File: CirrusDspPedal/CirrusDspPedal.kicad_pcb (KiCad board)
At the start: 2 copper layers, 112.5 x 86.4 mm, 89 parts, among them J1 MonoJack2Switch, J2 MonoJack2Switch, J3 Conn_02x05_Odd_Even, J4 Barrel_Jack_Switch, J5 MonoJack2Switch, J6 Micro_SD_Card_Det, J7 Conn_01x01, K1 HFD4/5-S, SW1 P26L-1D-RND MTL, SW2 P26L-1D-RND MTL, SW3 SW_SPST, SW4 SW_SPST, U1 CS5343, U2 74AHC1G126, U3 CS4344, U5 MCP1703T-3302E/CB, U6 MCP601-xOT, U7 STM32F405RGTx

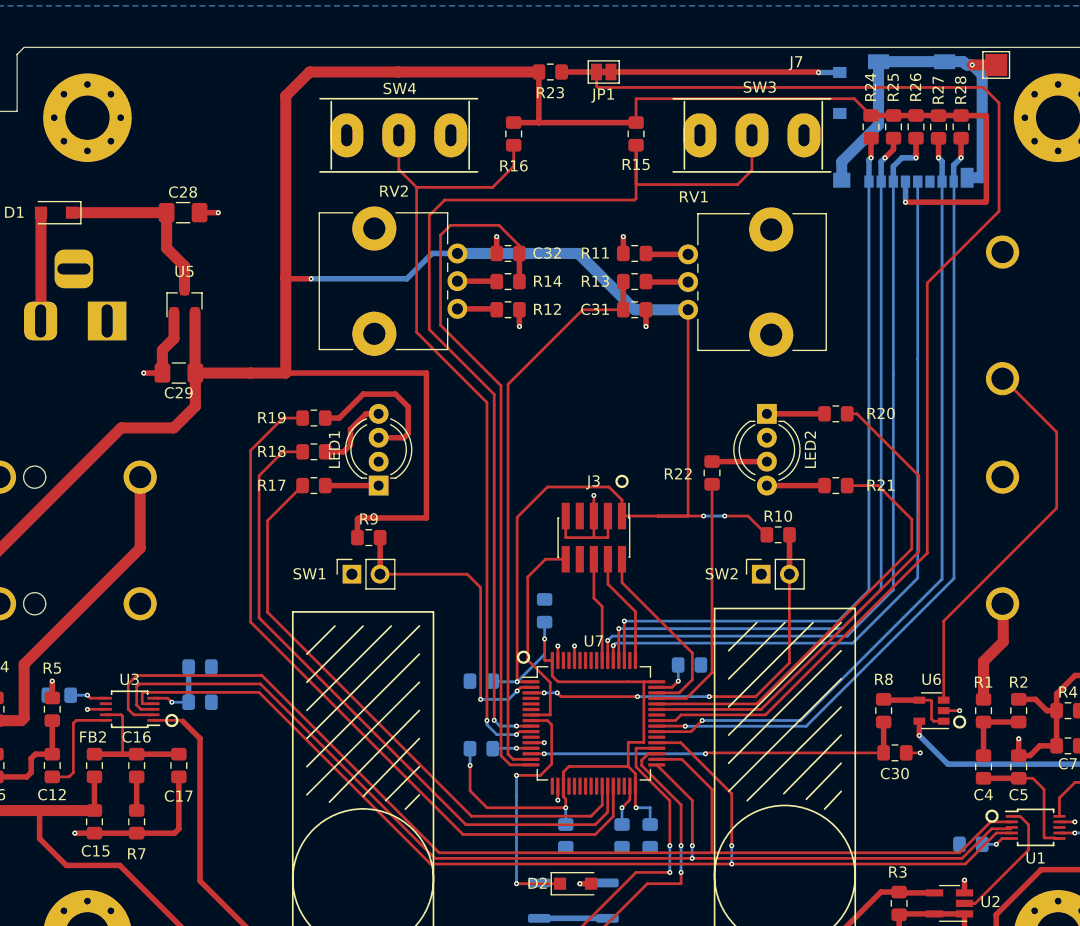
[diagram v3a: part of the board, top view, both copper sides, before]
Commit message: updated design and layout
- Changed LDO package from SOT23 to SOT223
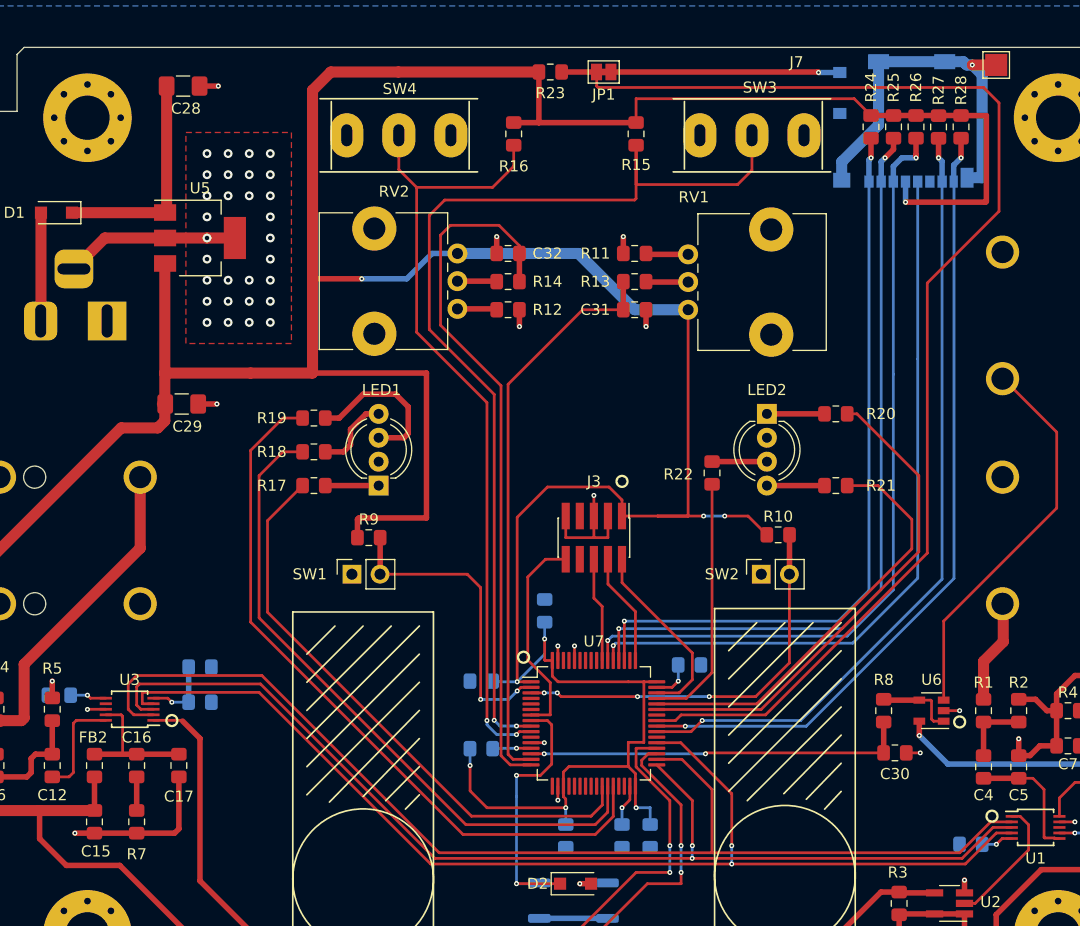
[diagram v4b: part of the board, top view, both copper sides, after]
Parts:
- U5: value MCP1703T-3302E/CB -> MCP1703A-1202_SOT223; footprint Package_TO_SOT_SMD:SOT-23 -> Package_TO_SOT_SMD:SOT-223-3_TabPin2
- moved C28 11.4 mm to (113.4, 58.0)
- moved U5 5.88 mm to (114.9, 71.8), turned to 0 degrees
- moved C29 2.81 mm to (113.3, 86.7), turned to 0 degrees
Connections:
- U5 pad 1: GND -> Net-(C28-Pad1)
- U5 pad 2: +3V3 -> GND
- U5 pad 3: Net-(C28-Pad1) -> +3V3
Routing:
- net GND: track 77.6 -> 87.4 mm, vias 22 -> 52
- net Net-(C28-Pad1): track 16.2 -> 19.9 mm
- net +3V3: track 562.4 -> 565.7 mm
- added copper zone on F.Cu, net GND

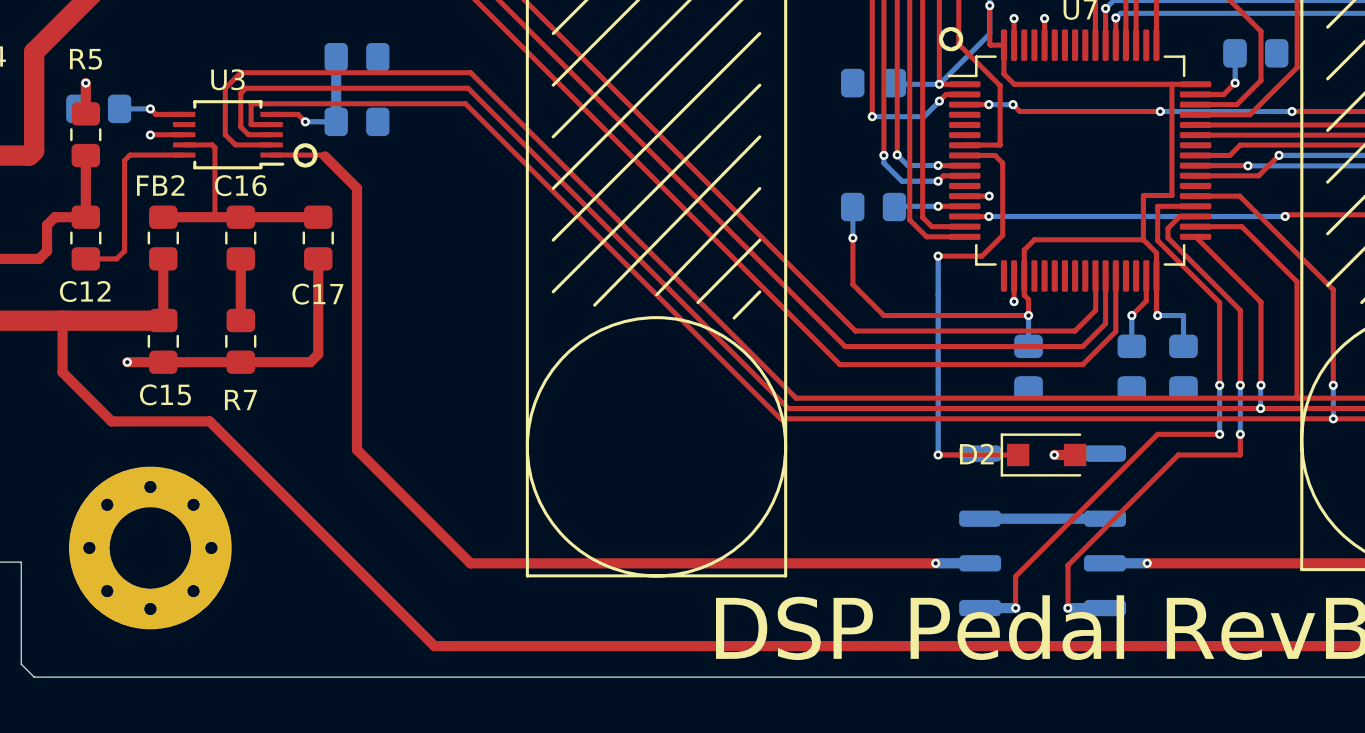
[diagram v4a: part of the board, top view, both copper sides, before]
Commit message: Updated design
- Corrected trace going to wrong CS4344 channel output
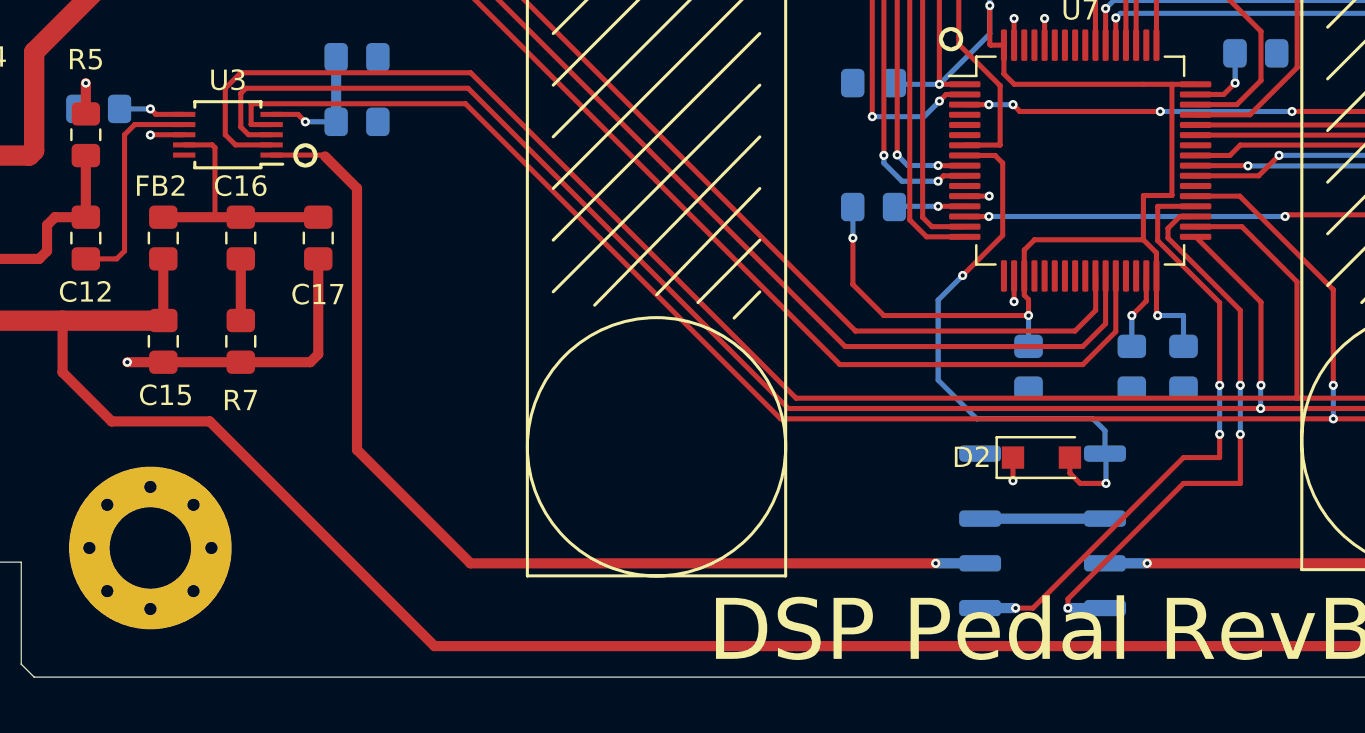
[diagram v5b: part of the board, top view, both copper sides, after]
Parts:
- moved D2 0.28 mm to (148.6, 130.2)
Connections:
- D2 pad 1: /SignalProcessing/RelayCoil_OUT -> GND
- D2 pad 2: GND -> /SignalProcessing/RelayCoil_OUT
- K1 pad 1: GND -> /SignalProcessing/RelayCoil_OUT
- K1 pad 8: /SignalProcessing/RelayCoil_OUT -> GND
- U3 pad 10: Net-(C12-Pad2) -> Net-(U3-Pad10)
- U3 pad 7: Net-(U3-Pad7) -> Net-(C12-Pad2)
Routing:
- net /SignalProcessing/RelayCoil_OUT: track 25.3 -> 28.9 mm
- net Net-(C12-Pad2): track 9.55 -> 10.9 mm

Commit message: finished revb layout
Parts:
- added C23: 1uF, Capacitor_SMD:C_1206_3216Metric_Pad1.42x1.75mm_HandSolder, F.Cu at (95.2, 87.6)
- added C24: 1uF, Capacitor_SMD:C_1206_3216Metric_Pad1.42x1.75mm_HandSolder, F.Cu at (104.1, 87.6)
- added U4: SE8250X2_SOT23, Package_TO_SOT_SMD:SOT-23, F.Cu at (99.7, 87.6)
- C18, C19, C21, C22, C33: moved to F.Cu
- K1: value HFD4/5-S -> HFD4/3_S
- moved C6 21.1 mm to (199.8, 124.1), turned to 270 degrees
- moved R3 17.7 mm to (195.3, 128.1), turned to 0 degrees
- moved U2 14.8 mm to (195.3, 124.4), turned to 270 degrees
- moved C30 14.3 mm to (180.8, 104.3), turned to 270 degrees
- moved C18 8.63 mm to (146.2, 105.4), turned to 90 degrees
- moved R8 7.40 mm to (180.8, 108.3), turned to 270 degrees
- moved C1 6.35 mm to (190.1, 123.1)
- moved C2 6.35 mm to (190.1, 125.5)
- moved C3 6.35 mm to (178.2, 126.5)
- moved U1 6.35 mm to (184.0, 125.0)
- moved C33 3.82 mm to (156.3, 107.7), turned to 270 degrees
- moved C21 2.67 mm to (148.7, 105.4)
- moved C12 2.54 mm to (104.1, 119.4)
- moved C13 2.54 mm to (104.8, 113.0)
- moved C14 2.54 mm to (99.1, 114.3)
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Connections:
- C15 pad 1: +3V3 -> +5V
- C6 pad 1: +3V3 -> +5V
- C7 pad 1: +3V3 -> +5V
- FB1 pad 2: +3V3 -> +5V
- FB2 pad 2: +3V3 -> +5V
- R3 pad 2: +3V3 -> +5V
- U2 pad 1: +3V3 -> +5V
- U2 pad 5: +3V3 -> +5V
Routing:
- net +5V: track 0.00 -> 183.5 mm, vias 0 -> 2
- net +3V3: track 565.7 -> 393.7 mm, vias 12 -> 13
- net Net-(C23-Pad1): track 19.9 -> 53.7 mm
- net /InputSignal/ADIN_LRCK: track 99.9 -> 131.7 mm
- net /InputSignal/ADIN_SCLK: track 104.5 -> 135.7 mm
- net /InputSignal/ADIN_MCLK: track 103.1 -> 132.8 mm, vias 2 -> 5
- net /ExtInput/FootExp_IN: track 34.9 -> 61.2 mm
- net GND: track 87.5 -> 113.1 mm, vias 52 -> 56
- net /InputSignal/ADIN_SDOUT: track 31.5 -> 52.9 mm
- net /InputSignal/SDOUT: track 11.9 -> 22.3 mm
- net /MicroSD/uSD_CMD: track 71.8 -> 62.3 mm
- net /MicroSD/uSD_D3: track 69.2 -> 60.6 mm
- net /MicroSD/uSD_CLK: track 67.1 -> 58.6 mm
- net /SignalProcessing/LEDA_R: track 52.7 -> 61.3 mm
- net /MicroSD/uSD_D2: track 67.9 -> 59.8 mm
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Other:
- outline, holes or cut-outs redrawn

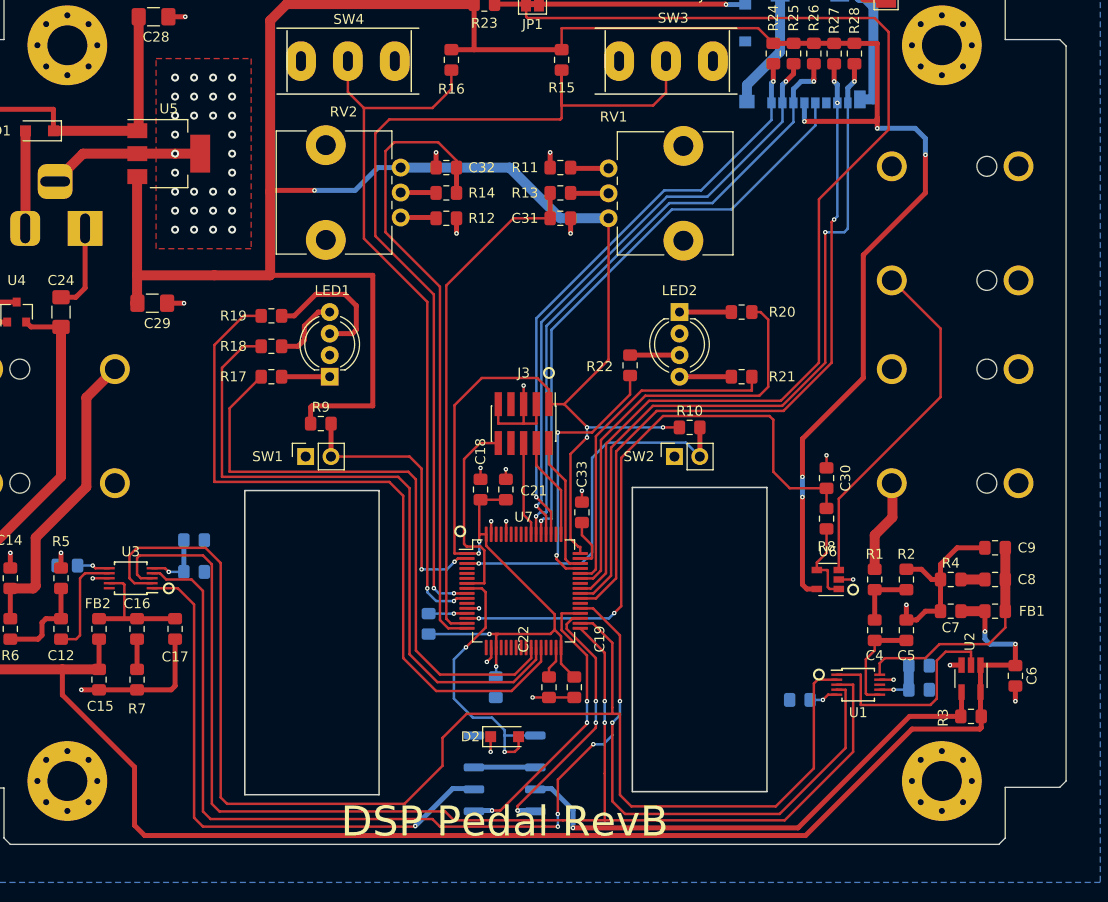
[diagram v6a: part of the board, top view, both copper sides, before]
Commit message: updated revb
- Added n-chan and 5V/3V3 jumper for relay
- Moved MCU to the middle of PCB (more space)
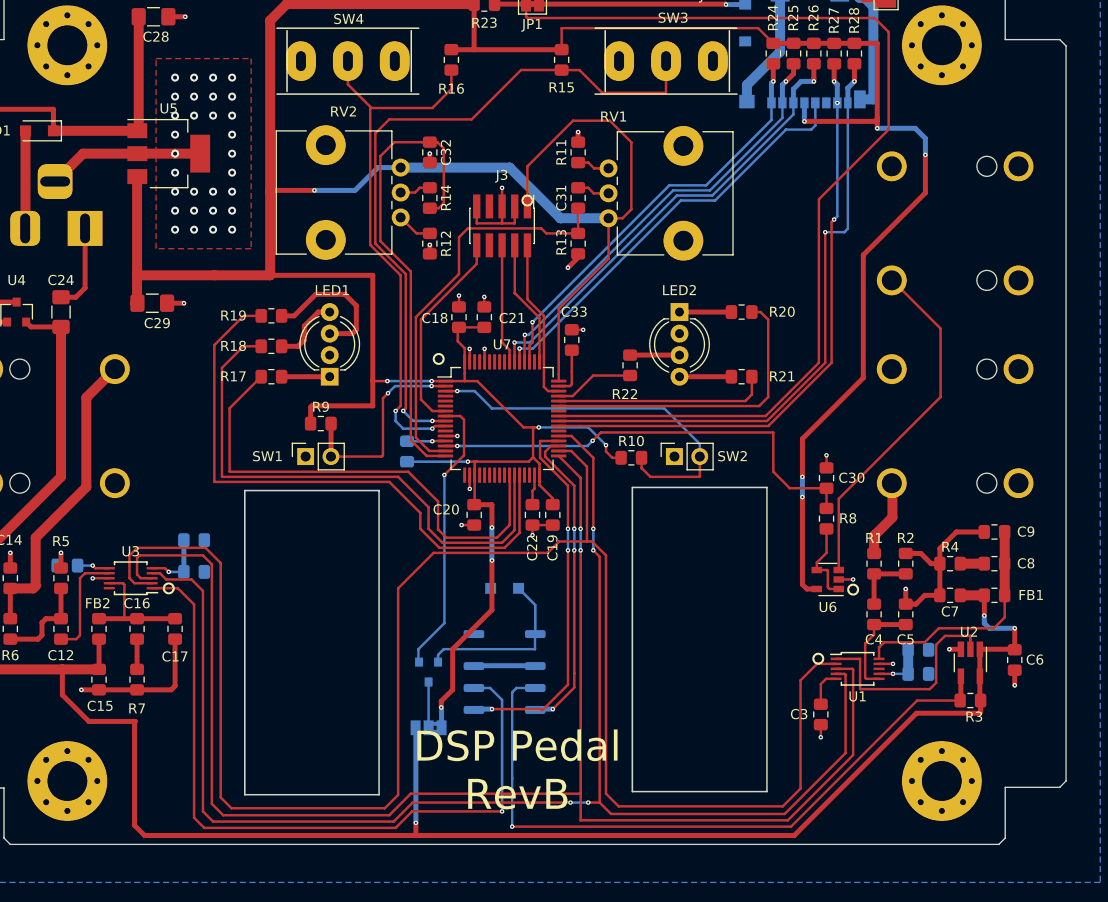
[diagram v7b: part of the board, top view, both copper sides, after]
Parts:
- added JP2: Jumper_3_Bridged12, Jumper:SolderJumper-3_P1.3mm_Bridged2Bar12_Pad1.0x1.5mm, B.Cu at (141.0, 129.3)
- added Q1: DMG2302U, Package_TO_SOT_SMD:SOT-23, B.Cu at (141.0, 123.7)
- C20, C3: moved to F.Cu
- D2: moved to B.Cu
- moved J3 19.9 mm to (148.3, 79.0)
- moved L1 17.4 mm to (138.8, 101.6)
- moved C21 17.4 mm to (146.6, 88.1)
- moved C18 17.4 mm to (144.0, 88.1)
- moved C19 17.4 mm to (153.4, 108.0)
- moved C20 17.4 mm to (145.5, 108.0)
- moved U7 17.4 mm to (148.3, 98.3)
- moved C22 17.4 mm to (151.4, 108.0)
- moved C33 17.3 mm to (155.3, 90.4)
- moved D2 14.9 mm to (148.6, 115.3), turned to 180 degrees
- moved K1 10.2 mm to (148.6, 123.7)
- moved R10 6.59 mm to (161.3, 102.2)
- moved C31 3.10 mm to (156.0, 80.8), turned to 90 degrees
- moved R12 3.03 mm to (141.1, 80.8), turned to 270 degrees
- moved C3 2.55 mm to (180.3, 128.0), turned to 270 degrees
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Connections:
- D2 pad 1: GND -> Net-(D2-Pad1)
- D2 pad 2: /SignalProcessing/RelayCoil_OUT -> GND
- K1 pad 1: /SignalProcessing/RelayCoil_OUT -> Net-(D2-Pad1)
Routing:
- net /InputSignal/ADIN_SCLK: track 135.7 -> 171.9 mm
- net /ExtInput/UserSwitchA_IN: track 93.4 -> 69.7 mm
- net /InputSignal/ADIN_LRCK: track 131.7 -> 151.4 mm
- net /SignalProcessing/LEDB_B: track 26.2 -> 8.00 mm, vias 2 -> 0
- net /ExtInput/UserSwitchB_IN: track 72.4 -> 54.7 mm
- net /MicroSD/uSD_D2: track 59.8 -> 42.2 mm
- net Net-(D2-Pad1): track 0.00 -> 17.5 mm
- net /MicroSD/uSD_D3: track 60.6 -> 43.4 mm
- net /OutputSignal/ADOUT_SDIN: track 56.3 -> 72.7 mm
- net /MicroSD/uSD_CMD: track 62.3 -> 46.0 mm
- net /MicroSD/uSD_CLK: track 58.6 -> 42.5 mm
- net /InputSignal/ADIN_SDOUT: track 52.9 -> 68.7 mm
- net /ExtInput/FootExp_IN: track 61.2 -> 45.4 mm
- net /ExtInput/UserPotB_IN: track 63.8 -> 48.8 mm
- net +5V: track 183.5 -> 197.7 mm, vias 2 -> 3
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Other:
- board text added: "3V3"
- board text added: "5V"
